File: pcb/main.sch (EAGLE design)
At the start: 53 parts, among them J3 455-1750-1-ND, J6 M1 connector, J7 M2 connector, Q1 2.5A/30V/105mΩ, U1 LSM303C, U5 ESP-WROOM-32

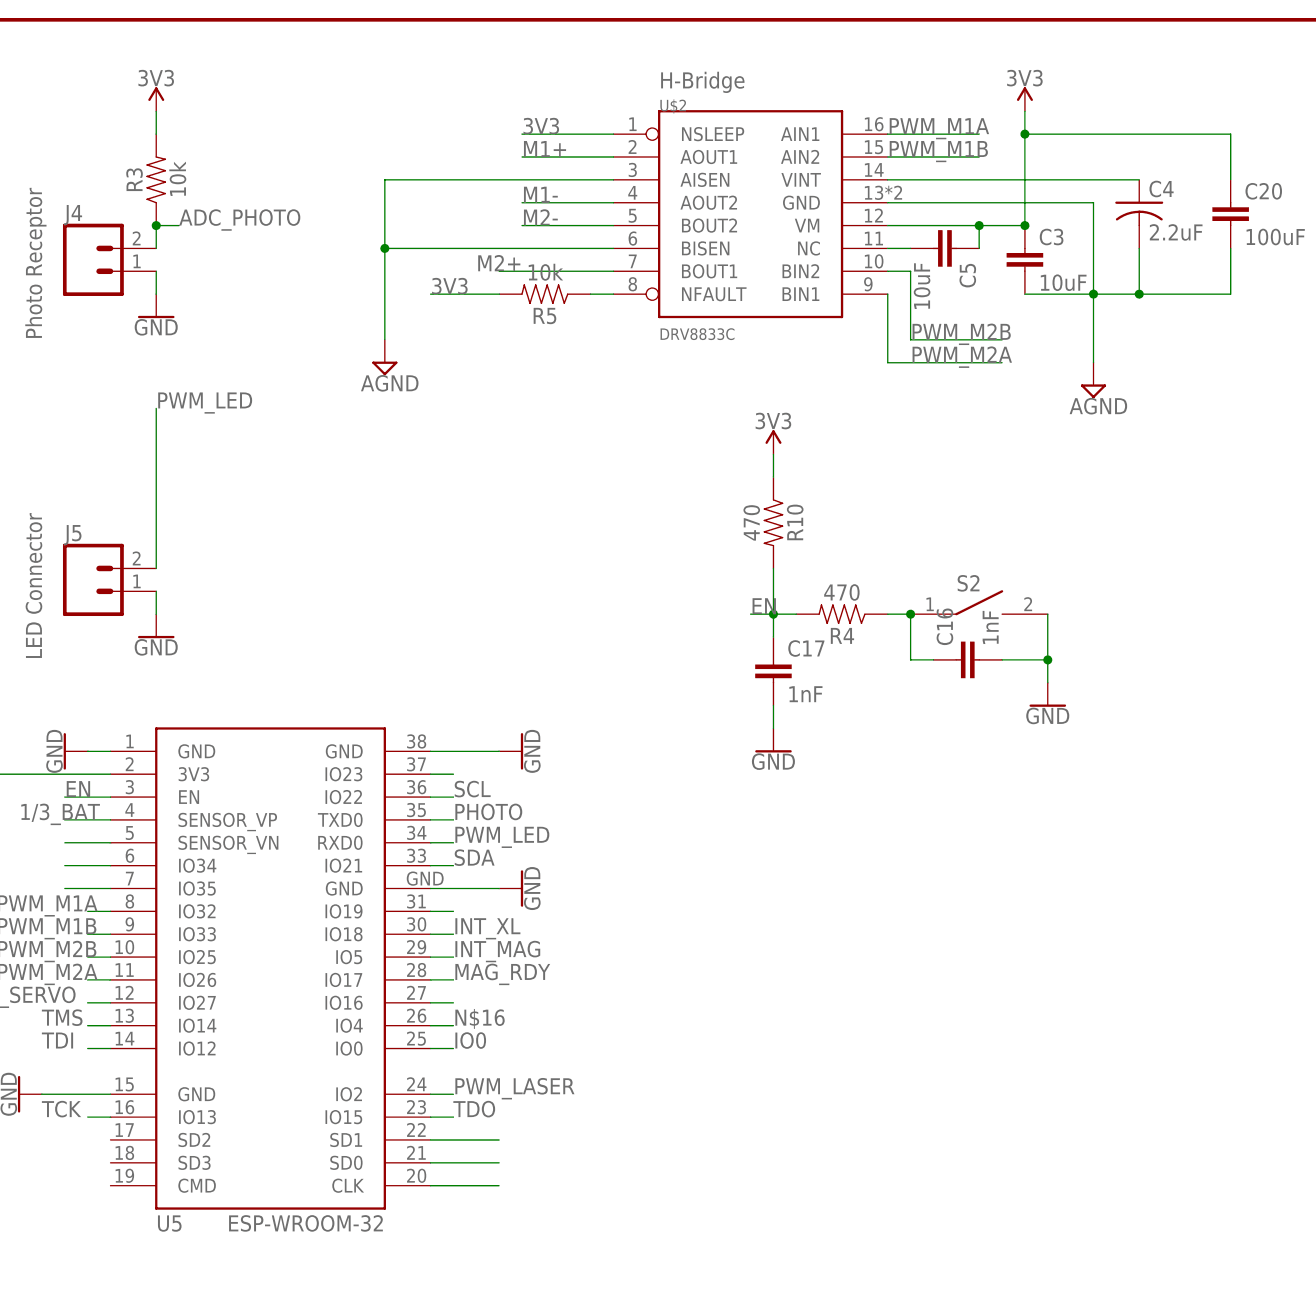
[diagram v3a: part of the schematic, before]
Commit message: added schmitt trigger
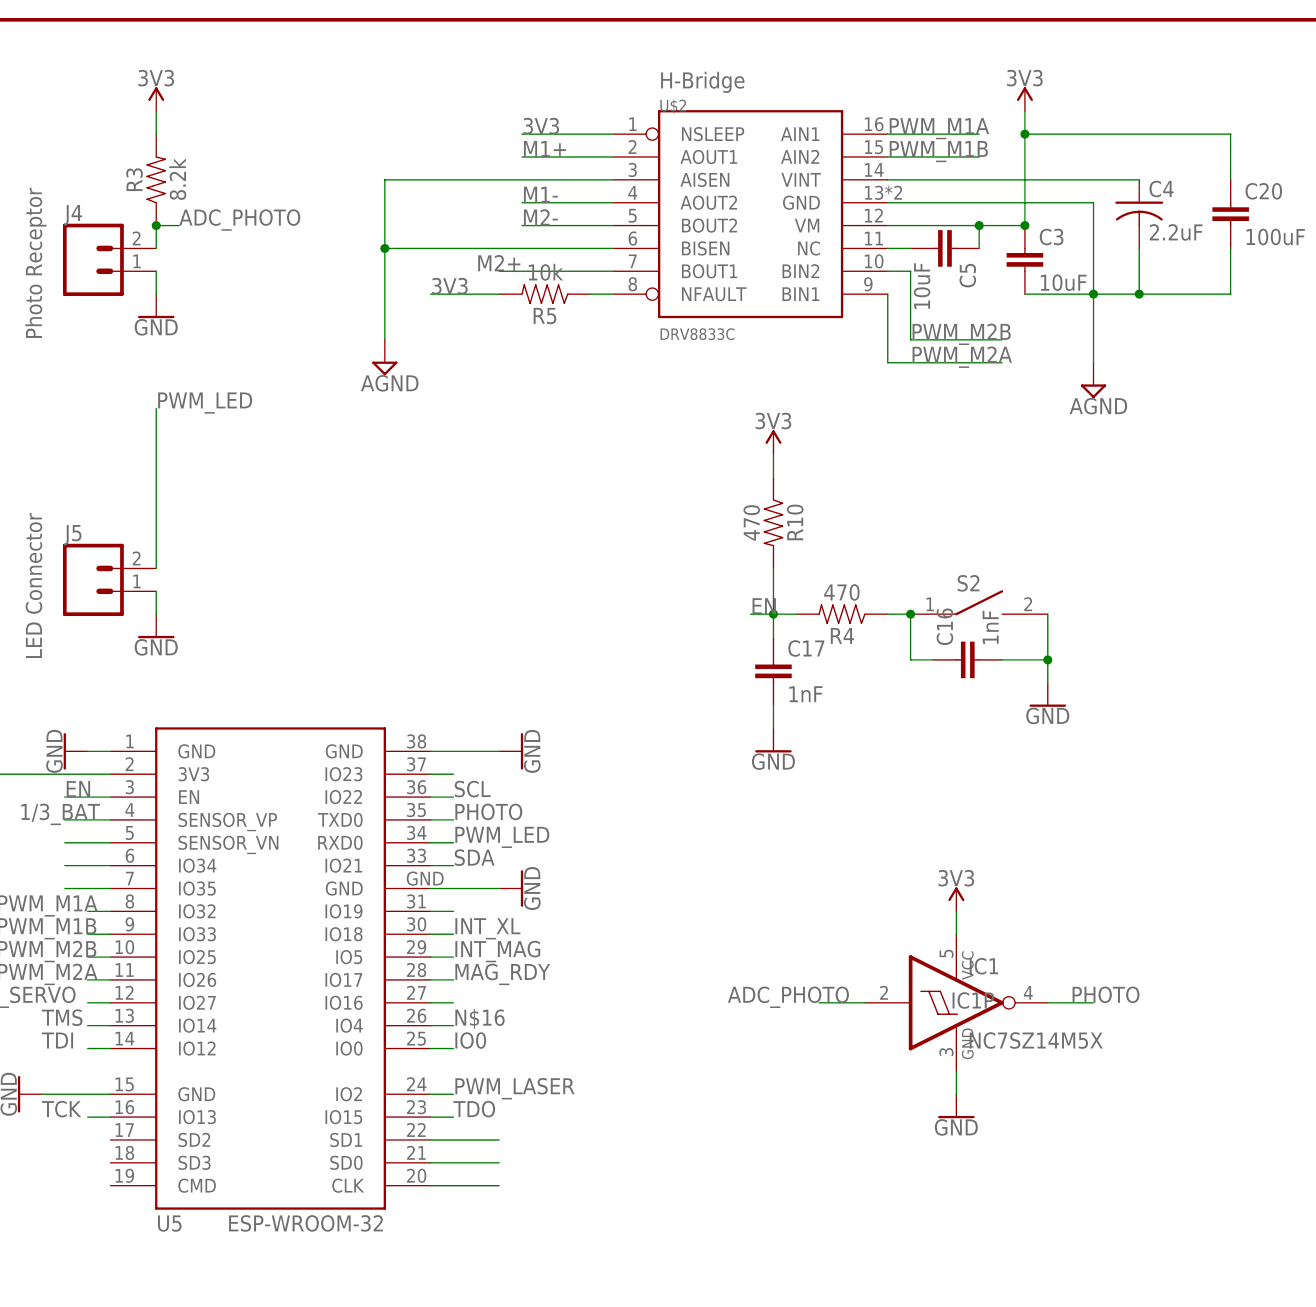
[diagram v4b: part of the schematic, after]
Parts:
- added IC1: NC7SZ14M5X, electricSheepParty:NC7SZ14M5X
- R3: value 10k -> 8.2k
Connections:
- net ADC_PHOTO: now also IC1Q.I
- net GND: now also IC1P.GND
- net PHOTO: now also IC1Q.O
- net VCC: now also IC1P.VCC
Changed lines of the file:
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@@
 <?xml version="1.0" encoding="utf-8"?>
 <!DOCTYPE eagle SYSTEM "eagle.dtd">
-<eagle version="8.3.2">
+<eagle version="8.6.0">
 <drawing>
 <settings>
@@
 <setting verticaltext="up"/>
 </settings>
-<grid distance="0.1" unitdist="inch" unit="inch" style="lines" multiple="1" display="no" altdistance="0.01" altunitdist="inch" altunit="inch"/>
+<grid distance="0.1" unitdist="inch" unit="inch" style="lines" multiple="1" display="yes" altdistance="0.01" altunitdist="inch" altunit="inch"/>
 <layers>
 <layer number="1" name="Top" color="4" fill="1" visible="no" active="no"/>
@@
 </part>
 <part name="SUPPLY4" library="SparkFun-PowerSymbols" deviceset="VCC" device="" value="3V3"/>
-<part name="R3" library="electricSheepParty" deviceset="RESISTOR" device="0603" value="10k"/>
+<part name="R3" library="electricSheepParty" deviceset="RESISTOR" device="0603" value="8.2k"/>
 <part name="C1" library="electricSheepParty" deviceset="0.1UF" device="-0603-25V-(+80/-20%)" value="0.1uF"/>
 <part name="C2" library="electricSheepParty" deviceset="0.1UF" device="-0603-25V-(+80/-20%)" value="0.1uF"/>
@@
 <part name="SUPPLY21" library="supply2" library_urn="urn:adsk.eagle:library:372" deviceset="AGND" device=""/>
 <part name="C20" library="eagle-ltspice" library_urn="urn:adsk.eagle:library:217" deviceset="C" device="C1206" package3d_urn="urn:adsk.eagle:package:13279/1" value="100uF"/>
+<part name="IC1" library="electricSheepParty" deviceset="NC7SZ14" device="M5X"/>
+<part name="GND4" library="SparkFun-PowerSymbols" deviceset="GND" device=""/>
+<part name="SUPPLY22" library="SparkFun-PowerSymbols" deviceset="VCC" device="" value="3V3"/>
 </parts>
 <sheets>
@@
 <instance part="SUPPLY21" gate="G$1" x="142.24" y="147.32"/>
 <instance part="C20" gate="G$1" x="236.22" y="165.1"/>
+<instance part="IC1" gate="Q" x="205.74" y="76.2"/>
+<instance part="IC1" gate="P" x="205.74" y="76.2"/>
+<instance part="GND4" gate="1" x="205.74" y="63.5"/>
+<instance part="SUPPLY22" gate="G$1" x="205.74" y="86.36"/>
 </instances>
 <busses>
@@
 <pinref part="GND3" gate="1" pin="GND"/>
 </segment>
+<segment>
+<pinref part="IC1" gate="P" pin="GND"/>
+<wire x1="205.74" y1="68.58" x2="205.74" y2="66.04" width="0.1524" layer="91"/>
+<pinref part="GND4" gate="1" pin="GND"/>
+</segment>
 </net>
 <net name="5V" class="0">
@@
 <junction x="116.84" y="162.56"/>
 <label x="119.38" y="162.56" size="1.778" layer="95"/>
+</segment>
+<segment>
+<pinref part="IC1" gate="Q" pin="I"/>
+<wire x1="195.58" y1="76.2" x2="190.5" y2="76.2" width="0.1524" layer="91"/>
+<label x="180.34" y="76.2" size="1.778" layer="95"/>
 </segment>
 </net>
@@
 <junction x="91.44" y="101.6"/>
 </segment>
+<segment>
+<pinref part="IC1" gate="P" pin="VCC"/>
+<wire x1="205.74" y1="83.82" x2="205.74" y2="86.36" width="0.1524" layer="91"/>
+<pinref part="SUPPLY22" gate="G$1" pin="VCC"/>
+</segment>
 </net>
 <net name="EN" class="0">
@@
 <label x="149.86" y="96.52" size="1.778" layer="95"/>
 </segment>
-</net>
+<segment>
+<pinref part="IC1" gate="Q" pin="O"/>
+<wire x1="215.9" y1="76.2" x2="220.98" y2="76.2" width="0.1524" layer="91"/>
+<label x="218.44" y="76.2" size="1.778" layer="95"/>
+</segment>
+</net>

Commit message: finished schematic (draft1)
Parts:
- removed FB1: (no value), rcl:R-EU_R0603
- added C21, C22: 10uF, rcl:C-EUC0805
- added C23: 0.1uF, electricSheepParty:0.1UF-0603-25V-(+80/-20%)
- added D4: red, electricSheepParty:LED0603
- added D5: green, electricSheepParty:LED0603
- added FB2: (no value), rcl:R-EU_R0603
- added JP1: (no value), pinhead:PINHD-1X5
- added R11, R12: 330, electricSheepParty:RESISTOR0603
- added TP1, TP10, TP11, TP12, TP13, TP14, TP2, TP3, TP4, TP5, TP6, TP7, TP8, TP9: TPPAD1-17, testpad:TPPAD1-17
- added U$5: SC1202-3.3V, carolyn:SC1202-3.3V
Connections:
- removed net IO0: U5.IO0
- new net 3V3M: C10.+, C11.1, C9.+, U$3.FB, U$4.P$2
- new net N$20: TP11.TP, U5.SD2
- new net N$21: TP12.TP, U5.SD3
- new net N$22: TP13.TP, U5.CMD
- new net N$25: D4.C, R11.2
- new net N$26: D5.C, R12.2
- new net N$27: TP14.TP, U5.IO0
- net 3V3: now also C21.1, C23.1, U$5.TAB, U$5.VOUT; no longer C10.+, C11.1, C9.+, U$3.FB, U$4.P$2
- net 6V: now also C22.1, U$5.VIN
- net AGND: now also C22.2, FB2.1, U$5.GND; no longer FB1.1
- net GND: now also C21.2, C23.2, FB2.2, JP1.5, R11.1, R12.1; no longer FB1.2
- net N$14: now also TP1.TP
- net N$15: now also TP9.TP
- net N$16: now also D4.A, TP10.TP
- net N$17: now also TP8.TP
- net N$18: now also TP7.TP
- net N$19: now also D5.A, TP6.TP
- net N$23: now also TP5.TP
- net N$24: now also TP4.TP
- net N$4: now also TP2.TP
- net N$5: now also TP3.TP
- net TCK: now also JP1.3
- net TDI: now also JP1.2
- net TDO: now also JP1.4
- net TMS: now also JP1.1
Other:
- note added: "6-3.3V linear reg"
- note added: "JTAG Header"
- note added: "schmidt trigger"
- moved on the sheet: C18, C19, IC1, IC1P, J1, J2, J5, Q2, U5

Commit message: layout done! (minus sheep image)
Still need to add sheep and check with tolerances of wherever we fab at,
but otherwise done!!!!
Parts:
- removed C12: 0.1uF, electricSheepParty:0.1UF-0603-25V-(+80/-20%)
- removed R6, R7: 10k, electricSheepParty:RESISTOR0603
- removed U1: LSM303C, SparkFun-Sensors:LSM303C
- added C24: 4.7uF, electricSheepParty:0.1UF-0603-25V-(+80/-20%)
- added IC2: LSM303DLHC, st-microelectronics:LSM303DLHC
- added R13, R14: 10k, electricSheepParty:RESISTOR0603
- added TP15, TP16, TP17, TP20: TPPAD1-13, testpad:TPPAD1-13
- C11: value 10uF -> 0.1uF; device rcl:C-EUC0805 -> electricSheepParty:0.1UF-0603-25V-(+80/-20%)
- C13: value 0.1uF -> 10uF; device electricSheepParty:0.1UF-0603-25V-(+80/-20%) -> rcl:C-EUC0805
- C14: value 10uF -> 0.22uF; device rcl:C-EUC0805 -> electricSheepParty:0.1UF-0603-25V-(+80/-20%)
- R1: value 1M -> 100k
- R8: value 20k -> 2k
- R9: value 10k -> 1k
- TP1, TP10, TP11, TP12, TP13, TP14, TP2, TP3, TP4, TP5, TP6, TP7, TP8, TP9: value TPPAD1-17 -> TPPAD1-13; device testpad:TPPAD1-17 -> testpad:TPPAD1-13
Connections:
- removed net INT_MAG: U1.INT_MAG, U5.IO5
- removed net INT_XL: U1.INT_XL, U5.IO18
- removed net MAG_RDY: U1.DRDY_MAG, U5.IO17
- removed net N$12: R6.2, R7.1, U1.CS_MAG, U1.CS_XL
- removed net N$6: C12.1, U1.C1
- removed net VCC: C18.1, C19.1, IC1P.VCC, U5.3V3
- new net DAT_RDY: IC2.DRDY, U5.IO17
- new net INT1: IC2.INT1, U5.IO5
- new net INT2: IC2.INT2, U5.IO18
- new net N$28: C14.2, IC2.SETC
- new net N$29: C14.1, IC2.SETP
- new net N$35: C24.1, IC2.C1
- net 3V3: now also C11.1, C18.1, C19.1, IC1P.VCC, IC2.VDD, IC2.VDD_IO, R13.1, R14.1, TP16.TP, U5.3V3; no longer C14.1, C20.1, C3.1, C5.1, R5.2, R7.2, U$2.NSLEEP, U$2.VM, U1.VDD, U1.VDD_IO
- net 3V3M: now also C20.1, C3.1, C5.1, R5.2, TP17.TP, U$2.NSLEEP, U$2.VM; no longer C11.1
- net AGND: now also TP10.TP; no longer C11.2
- net GND: now also C11.2, C24.2, IC2.GND, IC2.RSVD@1, IC2.RSVD@2, TP14.TP; no longer C12.2, C14.2, R6.1, U1.GND@1, U1.GND@2
- net N$14: now also TP3.TP; no longer TP1.TP
- net N$15: now also TP8.TP; no longer TP9.TP
- net N$16: now also TP5.TP; no longer TP10.TP
- net N$17: now also TP7.TP; no longer TP8.TP
- net N$18: now also TP15.TP; no longer TP7.TP
- net N$23: now also TP9.TP; no longer TP5.TP
- net N$27: now also TP20.TP; no longer TP14.TP
- net N$4: now also TP1.TP; no longer TP2.TP
- net N$5: now also TP2.TP; no longer TP3.TP
- net SCL: now also IC2.SLC, R13.2; no longer U1.SCL/SPC
- net SDA: now also IC2.SDA, R14.2; no longer U1.SDA/SDI/SDO
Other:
- note removed: "high for I2C"
- note removed: "low for SPI"
- moved on the sheet: C11, C13, C14, C21, C22, C23, FB2, TP1, TP10, TP14, TP2, TP3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

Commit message: added colors and finished constraining final model; organized schematic
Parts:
- RESET1: COMM (none) -> Reset Switch
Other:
- note added: "6-3.3V Lin Reg"
- note removed: "6-3.3V linear reg"
- moved on the sheet: C1, C10, C11, C13, C14, C15, C16, C17, C18, C19, C2, C20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
